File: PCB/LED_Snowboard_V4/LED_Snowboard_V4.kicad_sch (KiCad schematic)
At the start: 0 parts

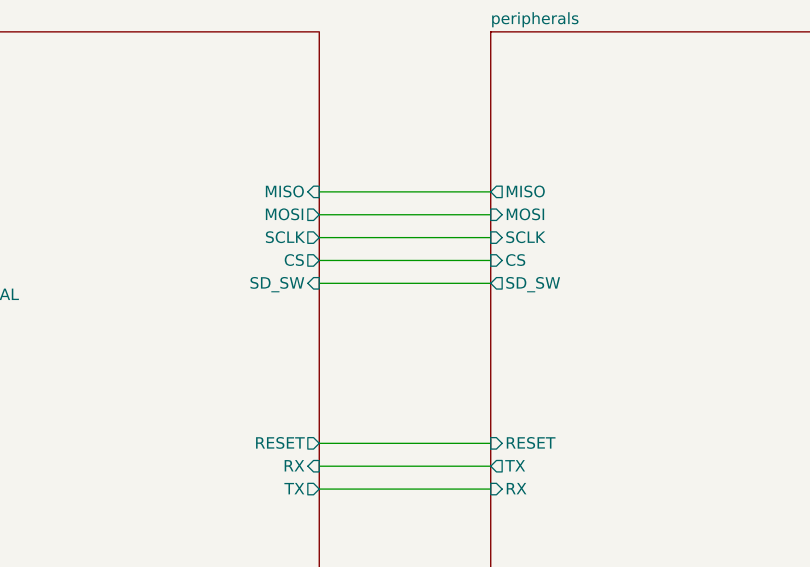
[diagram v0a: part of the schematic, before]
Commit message: Added Ram
Added Ram. need to finish DRC checks
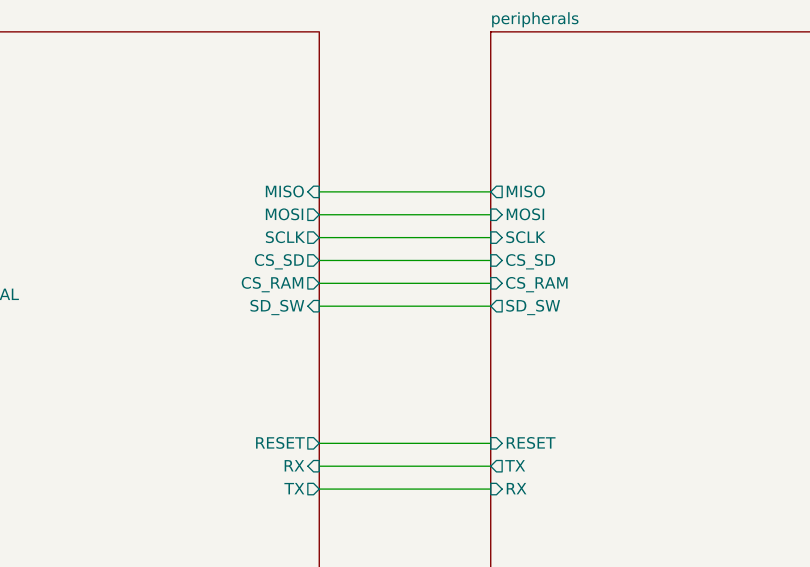
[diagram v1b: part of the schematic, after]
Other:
- sheet esp32 ports: added CS_RAM, CS_SD; removed CS
- sheet peripherals ports: added CS_RAM, CS_SD; removed CS
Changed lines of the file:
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@@
+    (stroke (width 0) (type default))
+  )
+  (wire (pts (xy 177.8 77.47) (xy 196.85 77.47))
+    (stroke (width 0) (type default))
+  )
+  (wire (pts (xy 111.76 105.41) (xy 123.19 105.41))
+    (stroke (width 0) (type default))
+  )
+  (wire (pts (xy 177.8 69.85) (xy 196.85 69.85))
+    (stroke (width 0) (type default))
+  )
+  (wire (pts (xy 196.85 121.92) (xy 187.96 121.92))
+    (stroke (width 0) (type default))
+  )
+  (wire (pts (xy 187.96 133.35) (xy 120.65 133.35))
+    (stroke (width 0) (type default))
+  )
+  (wire (pts (xy 177.8 97.79) (xy 196.85 97.79))
+    (stroke (width 0) (type default))
+  )
+  (wire (pts (xy 185.42 130.81) (xy 123.19 130.81))
+    (stroke (width 0) (type default))
+  )
+  (wire (pts (xy 111.76 76.2) (xy 130.81 76.2))
+    (stroke (width 0) (type default))
+  )
+  (wire (pts (xy 111.76 53.34) (xy 130.81 53.34))
+    (stroke (width 0) (type default))
+  )
+  (wire (pts (xy 111.76 92.71) (xy 130.81 92.71))
     (stroke (width 0) (type default))
   )
   (wire (pts (xy 177.8 74.93) (xy 196.85 74.93))
-    (stroke (width 0) (type default))
-  )
-  (wire (pts (xy 111.76 105.41) (xy 123.19 105.41))
-    (stroke (width 0) (type default))
-  )
-  (wire (pts (xy 177.8 69.85) (xy 196.85 69.85))
-    (stroke (width 0) (type default))
-  )
-  (wire (pts (xy 196.85 121.92) (xy 187.96 121.92))
-    (stroke (width 0) (type default))
-  )
-  (wire (pts (xy 187.96 133.35) (xy 120.65 133.35))
-    (stroke (width 0) (type default))
-  )
-  (wire (pts (xy 177.8 97.79) (xy 196.85 97.79))
-    (stroke (width 0) (type default))
-  )
-  (wire (pts (xy 185.42 130.81) (xy 123.19 130.81))
-    (stroke (width 0) (type default))
-  )
-  (wire (pts (xy 111.76 76.2) (xy 130.81 76.2))
-    (stroke (width 0) (type default))
-  )
-  (wire (pts (xy 111.76 53.34) (xy 130.81 53.34))
-    (stroke (width 0) (type default))
-  )
-  (wire (pts (xy 111.76 92.71) (xy 130.81 92.71))
     (stroke (width 0) (type default))
   )
@@
       (effects (font (size 1.27 1.27)) (justify left))
     )
-    (pin "SD_SW" output (at 196.85 74.93 180)
+    (pin "SD_SW" output (at 196.85 77.47 180)
       (effects (font (size 1.27 1.27)) (justify left))
     )
@@
       (effects (font (size 1.27 1.27)) (justify left))
     )
-    (pin "CS" input (at 196.85 72.39 180)
+    (pin "CS_SD" input (at 196.85 72.39 180)
       (effects (font (size 1.27 1.27)) (justify left))
     )
@@
     )
     (pin "RESET" input (at 196.85 92.71 180)
+      (effects (font (size 1.27 1.27)) (justify left))
+    )
+    (pin "CS_RAM" input (at 196.85 74.93 180)
       (effects (font (size 1.27 1.27)) (justify left))
     )
@@
       (effects (font (size 1.27 1.27)) (justify right))
     )
-    (pin "SD_SW" input (at 177.8 74.93 0)
+    (pin "SD_SW" input (at 177.8 77.47 0)
       (effects (font (size 1.27 1.27)) (justify right))
     )
@@
       (effects (font (size 1.27 1.27)) (justify right))
     )
-    (pin "CS" output (at 177.8 72.39 0)
+    (pin "CS_SD" output (at 177.8 72.39 0)
       (effects (font (size 1.27 1.27)) (justify right))
     )
@@
       (effects (font (size 1.27 1.27)) (justify left))
     )
+    (pin "CS_RAM" output (at 177.8 74.93 0)
+      (effects (font (size 1.27 1.27)) (justify right))
+    )
     (instances

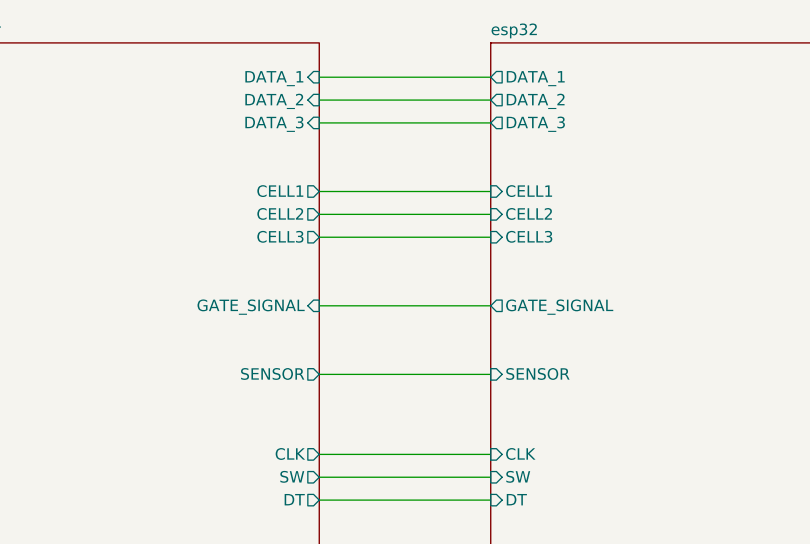
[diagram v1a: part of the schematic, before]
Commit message: updated control pcb
updated to add high side switching as well as added voltage divider and adjusted layout
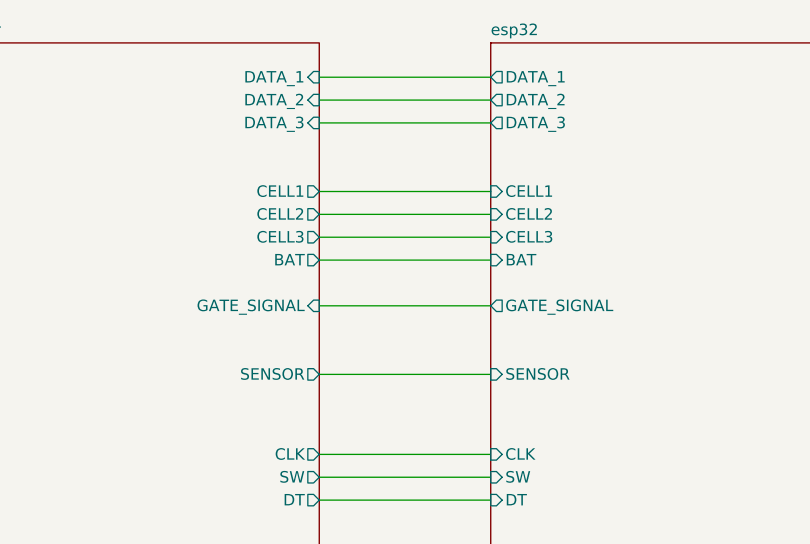
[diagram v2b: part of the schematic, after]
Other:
- sheet IO and Power ports: added BAT; removed none
- sheet esp32 ports: added BAT; removed none
